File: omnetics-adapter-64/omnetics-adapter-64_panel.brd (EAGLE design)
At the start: 119 x 83 mm, 84 parts, among them J1 DF40-REC, J10 DF40-REC, J13 DF40-REC, J16 DF40-REC, J19 DF40-REC, J22 DF40-REC, J25 DF40-REC, J4 DF40-REC, J7 DF40-REC

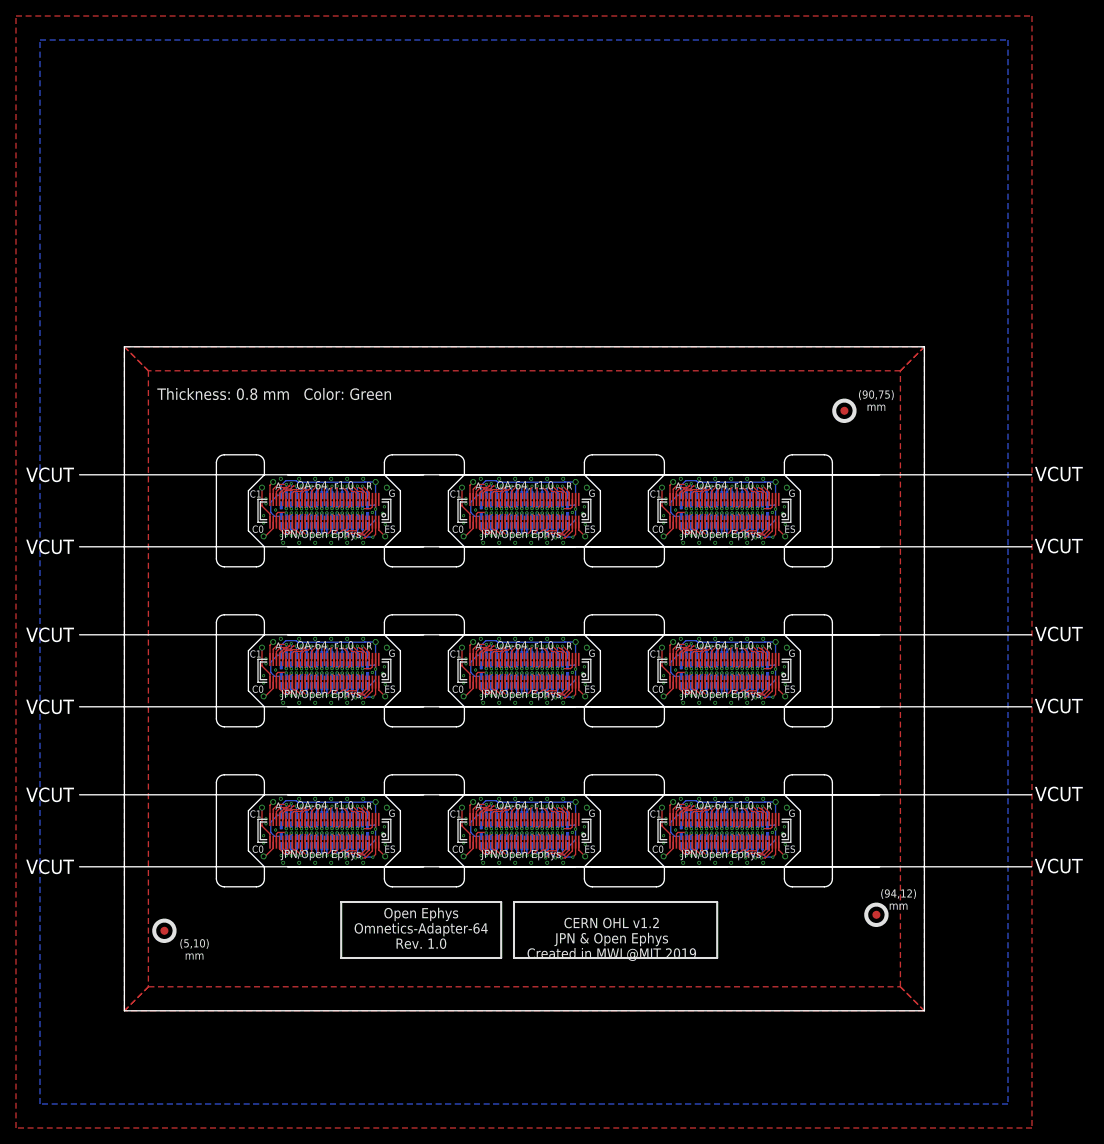
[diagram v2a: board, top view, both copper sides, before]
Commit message: headstage-64 rev. 1.4 along with all dependencies
- This is headstage-64 revision 1.4. Because it involves a change in the
bottom analog connector, a lot of other boards had to be changed to
match the new pinout. That is why there are so many files in this
commit. Changes in revision 1.4 and affects on other boards are as
follows:

1. The coaxial adapter board has been improved to allow a regulator to
sit on the daughter board. To do this, the filtered vcoax had to brought
back to the daughter board and then out again after regulation. Of
course this regulation can be bypassed simply by connecting these
contacts

2. Vcoax decoupling has been greatly improved to lower impedance of
power input. There is now 70 uF of decoupling capacitance on the
post-regulated vcoax.

3. The JTAG interface was changed to allow it to be enabled and disabled
by the programmer. This means that these pins are nominally used for
extra IO. The programmer now contains a jumper that allows it operate in
this new mode (closed) or legacy mode (open) for headstage-64 rev 1.3.

4. All of the serializers GPIO lines are now all routed to the FPGA.

5. The opto and estim circuits no longer share SPI lines so they can be
operated independently.

6. The analog routing to the intan chip has been changed such that the
electrode lines are shielded from vcoax, which was polluting the anlog
signals, by a ground pin. This means that eibs etc. need to respect this
new pinout. This is why eib-64, eib-64-large, nanoz-adapter,
omnetics-adapter-64, and test-board-64 have been changed.

7. The serializer on headstage-64 has been upgraded to DS90UB933-Q1
which has reduced back channel latencies, increased forward channel
bandwidth, and improved performance with
imperfect cabling.

8. There is a solder jumper on the bottom of headstage-64 to allow the
addition of an external resistor to AUXIN3 on the intan to allow it to
operate at lower bandwidths. This comes at the cost of not being able to
measure istim unless t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
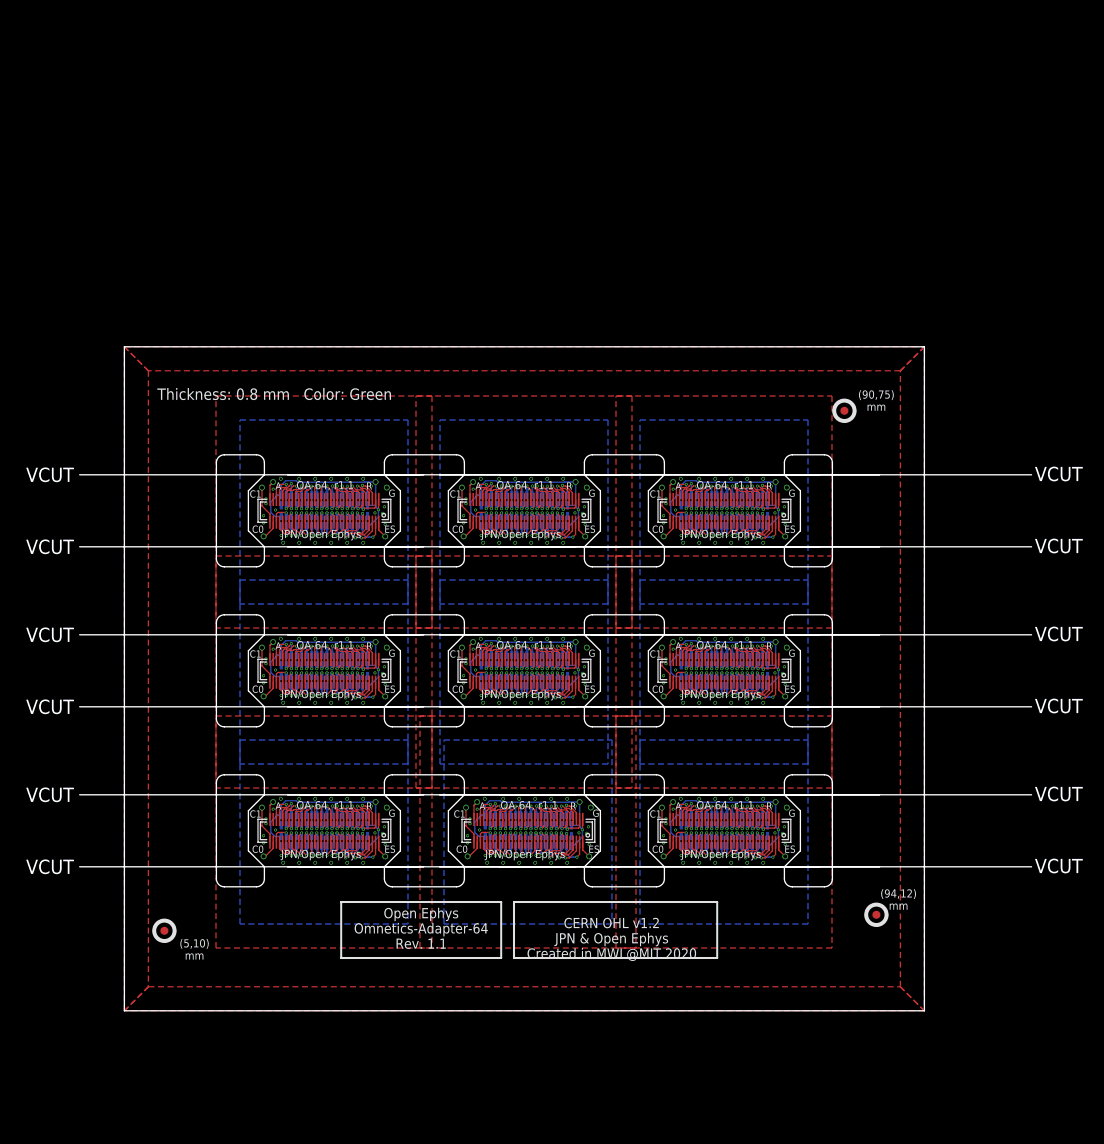
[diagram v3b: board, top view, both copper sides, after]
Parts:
- moved CAT12 50.0 mm to (67.4, 59.3)
- moved CAT16 50.0 mm to (17.4, 59.3)
- moved ESTIM19 50.0 mm to (81.4, 66.1)
- moved ESTIM25 50.0 mm to (31.4, 66.1)
- moved CAT13 50.0 mm to (67.2, 65.4)
- moved CAT17 50.0 mm to (17.2, 65.4)
- moved ESTIM20 50.0 mm to (82.8, 65.4)
- moved ESTIM26 50.0 mm to (32.8, 65.4)
- moved J19 50.0 mm to (75.0, 62.5)
- moved J25 50.0 mm to (25.0, 62.5)
- moved AN6 50.0 mm to (68.6, 66.1)
- moved AN8 50.0 mm to (18.6, 66.1)
- moved ESTIM18 50.0 mm to (82.6, 59.3)
- moved ESTIM24 50.0 mm to (32.6, 59.3)
- moved J20 50.0 mm to (69.6, 64.5)
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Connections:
- new net GND1: ESTIM2.P$1, J1.37, J2.18, J2.36, J3.18, J3.36
- new net GND2: ESTIM8.P$1, J7.37, J8.18, J8.36, J9.18, J9.36
- new net GND3: ESTIM11.P$1, J10.37, J11.18, J11.36, J12.18, J12.36
- new net GND4: ESTIM14.P$1, J13.37, J14.18, J14.36, J15.18, J15.36
- new net GND5: ESTIM17.P$1, J16.37, J17.18, J17.36, J18.18, J18.36
- new net GND6: ESTIM20.P$1, J19.37, J20.18, J20.36, J21.18, J21.36
- new net GND7: ESTIM23.P$1, J22.37, J23.18, J23.36, J24.18, J24.36
- new net GND8: ESTIM26.P$1, J25.37, J26.18, J26.36, J27.18, J27.36
- net GND: now also J4.37; no longer ESTIM11.P$1, ESTIM14.P$1, ESTIM17.P$1, ESTIM2.P$1, ESTIM20.P$1, ESTIM23.P$1, ESTIM26.P$1, ESTIM8.P$1, J1.70, J10.70, J11.18, J11.36, J12.18, J12.36, J13.70, J14.18, J14.36, J15.18, J15.36, J16.70, J17.18, J17.36, J18.18, J18.36, J19.70, J2.18, J2.36, J20.18, J20.36, J21.18, J21.36, J22.70, J23.18, J23.36, J24.18, J24.36, J25.70, J26.18, J26.36, J27.18, J27.36, J3.18, J3.36, J4.70, J7.70, J8.18, J8.36, J9.18, J9.36
- net N$1: now also J1.69; no longer J1.68
- net N$100: now also J4.38; no longer J4.37
- net N$12: now also J1.60; no longer J1.57
- net N$129: now also J7.69; no longer J7.68
- net N$130: now also J7.67; no longer J7.66
- net N$131: now also J7.65; no longer J7.64
- net N$132: now also J7.64; no longer J7.63
- net N$133: now also J7.63; no longer J7.62
- net N$135: now also J7.62; no longer J7.60
- net N$138: now also J7.60; no longer J7.57
- net N$14: now also J1.57; no longer J1.55
- net N$140: now also J7.57; no longer J7.55
- net N$142: now also J7.55; no longer J7.53
- net N$143: now also J7.53; no longer J7.52
- net N$144: now also J7.52; no longer J7.51
- net N$145: now also J7.51; no longer J7.50
- net N$146: now also J7.50; no longer J7.49
- net N$147: now also J7.49; no longer J7.48
- net N$148: now also J7.48; no longer J7.47
- net N$149: now also J7.47; no longer J7.46
- net N$150: now also J7.46; no longer J7.45
- net N$151: now also J7.45; no longer J7.44
- net N$152: now also J7.44; no longer J7.43
- net N$153: now also J7.43; no longer J7.42
- net N$154: now also J7.42; no longer J7.41
- net N$155: now also J7.41; no longer J7.40
- net N$156: now also J7.39; no longer J7.38
- net N$16: now also J1.55; no longer J1.53
- net N$161: now also J7.66; no longer J7.65
- net N$162: now also J7.68; no longer J7.67
- net N$163: now also J7.40; no longer J7.39
- net N$164: now also J7.38; no longer J7.37
- net N$17: now also J1.53; no longer J1.52
- net N$18: now also J1.52; no longer J1.51
- net N$19: now also J1.51; no longer J1.50
- net N$193: now also J10.69; no longer J10.68
- net N$194: now also J10.67; no longer J10.66
- net N$195: now also J10.65; no longer J10.64
- net N$196: now also J10.64; no longer J10.63
- net N$197: now also J10.63; no longer J10.62
- net N$199: now also J10.62; no longer J10.60
- net N$2: now also J1.66; no longer J1.65
- net N$20: now also J1.50; no longer J1.49
- net N$21: now also J1.49; no longer J1.48
- net N$22: now also J1.48; no longer J1.47
- net N$229: now also J10.60; no longer J10.57
- net N$23: now also J1.47; no longer J1.46
- net N$231: now also J10.57; no longer J10.55
- net N$233: now also J10.55; no longer J10.53
- net N$234: now also J10.53; no longer J10.52
- net N$235: now also J10.52; no longer J10.51
- net N$236: now also J10.51; no longer J10.50
- net N$237: now also J10.50; no longer J10.49
- net N$238: now also J10.49; no longer J10.48
- net N$239: now also J10.48; no longer J10.47
- net N$24: now also J1.46; no longer J1.45
- net N$240: now also J10.47; no longer J10.46
- net N$241: now also J10.46; no longer J10.45
- net N$242: now also J10.45; no longer J10.44
- net N$243: now also J10.44; no longer J10.43
- net N$244: now also J10.43; no longer J10.42
- net N$245: now also J10.42; no longer J10.41
- net N$246: now also J10.41; no longer J10.40
- net N$247: now also J10.39; no longer J10.38
- net N$25: now also J1.45; no longer J1.44
- net N$252: now also J10.66; no longer J10.65
- net N$253: now also J10.68; no longer J10.67
- net N$254: now also J10.40; no longer J10.39
- net N$255: now also J10.38; no longer J10.37
- net N$26: now also J1.44; no longer J1.43
- net N$27: now also J1.43; no longer J1.42
- net N$28: now also J1.42; no longer J1.41
- net N$284: now also J13.69; no longer J13.68
- net N$285: now also J13.67; no longer J13.66
- net N$286: now also J13.65; no longer J13.64
- net N$287: now also J13.64; no longer J13.63
- net N$288: now also J13.63; no longer J13.62
- net N$29: now also J1.41; no longer J1.40
- net N$290: now also J13.62; no longer J13.60
- net N$293: now also J13.60; no longer J13.57
- net N$295: now also J13.57; no longer J13.55
- net N$297: now also J13.55; no longer J13.53
- net N$298: now also J13.53; no longer J13.52
- net N$299: now also J13.52; no longer J13.51
- net N$3: now also J1.67; no longer J1.66
- net N$30: now also J1.40; no longer J1.39
- net N$300: now also J13.51; no longer J13.50
- net N$301: now also J13.50; no longer J13.49
- net N$302: now also J13.49; no longer J13.48
- net N$303: now also J13.48; no longer J13.47
- net N$304: now also J13.47; no longer J13.46
- net N$305: now also J13.46; no longer J13.45
- net N$306: now also J13.45; no longer J13.44
- net N$307: now also J13.44; no longer J13.43
- net N$308: now also J13.43; no longer J13.42
- net N$309: now also J13.42; no longer J13.41
- net N$31: now also J1.39; no longer J1.38
- net N$310: now also J13.41; no longer J13.40
- net N$311: now also J13.39; no longer J13.38
- net N$316: now also J13.66; no longer J13.65
- net N$317: now also J13.68; no longer J13.67
- net N$318: now also J13.40; no longer J13.39
- net N$319: now also J13.38; no longer J13.37
- net N$32: now also J1.38; no longer J1.37
- net N$348: now also J16.69; no longer J16.68
- net N$349: now also J16.67; no longer J16.66
- net N$350: now also J16.65; no longer J16.64
- net N$351: now also J16.64; no longer J16.63
- net N$352: now also J16.63; no longer J16.62
- net N$354: now also J16.62; no longer J16.60
- net N$357: now also J16.60; no longer J16.57
- net N$359: now also J16.57; no longer J16.55
- net N$361: now also J16.55; no longer J16.53
- net N$362: now also J16.53; no longer J16.52
- net N$363: now also J16.52; no longer J16.51
- net N$364: now also J16.51; no longer J16.50
- net N$365: now also J16.50; no longer J16.49
- net N$366: now also J16.49; no longer J16.48
- net N$367: now also J16.48; no longer J16.47
- net N$368: now also J16.47; no longer J16.46
- net N$369: now also J16.46; no longer J16.45
- net N$370: now also J16.45; no longer J16.44
- net N$371: now also J16.44; no longer J16.43
- net N$372: now also J16.43; no longer J16.42
- net N$373: now also J16.42; no longer J16.41
- net N$374: now also J16.41; no longer J16.40
- net N$375: now also J16.39; no longer J16.38
- net N$380: now also J16.66; no longer J16.65
- net N$381: now also J16.68; no longer J16.67
- net N$382: now also J16.40; no longer J16.39
- net N$383: now also J16.38; no longer J16.37
- net N$4: now also J1.68; no longer J1.67
- net N$412: now also J19.69; no longer J19.68
- net N$413: now also J19.67; no longer J19.66
- net N$414: now also J19.65; no longer J19.64
- net N$415: now also J19.64; no longer J19.63
- net N$416: now also J19.63; no longer J19.62
- net N$418: now also J19.62; no longer J19.60
- net N$421: now also J19.60; no longer J19.57
- net N$423: now also J19.57; no longer J19.55
- net N$425: now also J19.55; no longer J19.53
- net N$426: now also J19.53; no longer J19.52
- net N$427: now also J19.52; no longer J19.51
- net N$428: now also J19.51; no longer J19.50
- net N$429: now also J19.50; no longer J19.49
- net N$430: now also J19.49; no longer J19.48
- net N$431: now also J19.48; no longer J19.47
- net N$432: now also J19.47; no longer J19.46
- net N$433: now also J19.46; no longer J19.45
- net N$434: now also J19.45; no longer J19.44
- net N$435: now also J19.44; no longer J19.43
- net N$436: now also J19.43; no longer J19.42
- net N$437: now also J19.42; no longer J19.41
- net N$438: now also J19.41; no longer J19.40
- net N$439: now also J19.39; no longer J19.38
- net N$444: now also J19.66; no longer J19.65
- net N$445: now also J19.68; no longer J19.67
- net N$446: now also J19.40; no longer J19.39
- net N$447: now also J19.38; no longer J19.37
- net N$476: now also J22.69; no longer J22.68
- net N$477: now also J22.67; no longer J22.66
- net N$478: now also J22.65; no longer J22.64
- net N$479: now also J22.64; no longer J22.63
- net N$480: now also J22.63; no longer J22.62
- net N$482: now also J22.62; no longer J22.60
- net N$485: now also J22.60; no longer J22.57
- net N$487: now also J22.57; no longer J22.55
- net N$489: now also J22.55; no longer J22.53
- net N$490: now also J22.53; no longer J22.52
- net N$491: now also J22.52; no longer J22.51
- net N$492: now also J22.51; no longer J22.50
- net N$493: now also J22.50; no longer J22.49
- net N$494: now also J22.49; no longer J22.48
- net N$495: now also J22.48; no longer J22.47
- net N$496: now also J22.47; no longer J22.46
- net N$497: now also J22.46; no longer J22.45
- net N$498: now also J22.45; no longer J22.44
- net N$499: now also J22.44; no longer J22.43
- net N$5: now also J1.65; no longer J1.64
- net N$500: now also J22.43; no longer J22.42
- net N$501: now also J22.42; no longer J22.41
- net N$502: now also J22.41; no longer J22.40
- net N$503: now also J22.39; no longer J22.38
- net N$508: now also J22.66; no longer J22.65
- net N$509: now also J22.68; no longer J22.67
- net N$510: now also J22.40; no longer J22.39
- net N$511: now also J22.38; no longer J22.37
- net N$540: now also J25.69; no longer J25.68
- net N$541: now also J25.67; no longer J25.66
- net N$542: now also J25.65; no longer J25.64
- net N$543: now also J25.64; no longer J25.63
- net N$544: now also J25.63; no longer J25.62
- net N$546: now also J25.62; no longer J25.60
- net N$549: now also J25.60; no longer J25.57
- net N$551: now also J25.57; no longer J25.55
- net N$553: now also J25.55; no longer J25.53
- net N$554: now also J25.53; no longer J25.52
- net N$555: now also J25.52; no longer J25.51
- net N$556: now also J25.51; no longer J25.50
- net N$557: now also J25.50; no longer J25.49
- net N$558: now also J25.49; no longer J25.48
- net N$559: now also J25.48; no longer J25.47
- net N$560: now also J25.47; no longer J25.46
- net N$561: now also J25.46; no longer J25.45
- net N$562: now also J25.45; no longer J25.44
- net N$563: now also J25.44; no longer J25.43
- net N$564: now also J25.43; no longer J25.42
- net N$565: now also J25.42; no longer J25.41
- net N$566: now also J25.41; no longer J25.40
- net N$567: now also J25.39; no longer J25.38
- net N$572: now also J25.66; no longer J25.65
- net N$573: now also J25.68; no longer J25.67
- net N$574: now also J25.40; no longer J25.39
- net N$575: now also J25.38; no longer J25.37
- net N$6: now also J1.64; no longer J1.63
- net N$65: now also J4.69; no longer J4.68
- net N$66: now also J4.67; no longer J4.66
- net N$67: now also J4.65; no longer J4.64
- net N$68: now also J4.64; no longer J4.63
- net N$69: now also J4.63; no longer J4.62
- net N$7: now also J1.63; no longer J1.62
- net N$71: now also J4.62; no longer J4.60
- net N$74: now also J4.60; no longer J4.57
- net N$76: now also J4.57; no longer J4.55
- net N$78: now also J4.55; no longer J4.53
- net N$79: now also J4.53; no longer J4.52
- net N$80: now also J4.52; no longer J4.51
- net N$81: now also J4.51; no longer J4.50
- net N$82: now also J4.50; no longer J4.49
- net N$83: now also J4.49; no longer J4.48
- net N$84: now also J4.48; no longer J4.47
- net N$85: now also J4.47; no longer J4.46
- net N$86: now also J4.46; no longer J4.45
- net N$87: now also J4.45; no longer J4.44
- net N$88: now also J4.44; no longer J4.43
- net N$89: now also J4.43; no longer J4.42
- net N$9: now also J1.62; no longer J1.60
- net N$90: now also J4.42; no longer J4.41
- net N$91: now also J4.41; no longer J4.40
- net N$92: now also J4.39; no longer J4.38
- net N$97: now also J4.66; no longer J4.65
- net N$98: now also J4.68; no longer J4.67
- net N$99: now also J4.40; no longer J4.39
- net REF: now also J1.70; no longer J1.69
- net REF1: now also J4.70; no longer J4.69
- net REF2: now also J7.70; no longer J7.69
- net REF3: now also J10.70; no longer J10.69
- net REF4: now also J13.70; no longer J13.69
- net REF5: now also J16.70; no longer J16.69
- net REF6: now also J19.70; no longer J19.69
- net REF7: now also J22.70; no longer J22.69
- net REF8: now also J25.70; no longer J25.69
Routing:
- net N$437: track 3.48 -> 1.73 mm
- net N$90: track 3.48 -> 1.73 mm
- net N$373: track 3.48 -> 1.73 mm
- net N$154: track 3.48 -> 1.73 mm
- net N$28: track 3.48 -> 1.73 mm
- net N$565: track 3.48 -> 1.73 mm
- net N$501: track 3.48 -> 1.73 mm
- net N$245: track 3.48 -> 1.73 mm
- net N$309: track 3.48 -> 1.73 mm
- net N$241: track 2.81 -> 1.59 mm
- net N$561: track 2.81 -> 1.59 mm
- net N$305: track 2.81 -> 1.59 mm
- net N$497: track 2.81 -> 1.59 mm
- net N$369: track 2.81 -> 1.59 mm
- net N$150: track 2.81 -> 1.59 mm
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- added copper zone on layer 1, net GND1
- added copper zone on layer 16, net GND1
- added copper zone on layer 1, net GND2
- added copper zone on layer 16, net GND2
- added copper zone on layer 1, net GND3
- added copper zone on layer 16, net GND3
- added copper zone on layer 1, net GND4
- added copper zone on layer 16, net GND4
- added copper zone on layer 1, net GND5
- added copper zone on layer 16, net GND5
- added copper zone on layer 1, net GND6
- added copper zone on layer 16, net GND6
- added copper zone on layer 1, net GND7
- added copper zone on layer 16, net GND7
- added copper zone on layer 1, net GND8
- added copper zone on layer 16, net GND8
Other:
- board text added: "CERN OHL v1.2 JPN & Open Ephys Created in MWL@MIT 2020"
- board text added: "OA-64, r1.1"
- board text added: "Open Ephys Omnetics-Adapter-64 Rev. 1.1"
- board text removed: "CERN OHL v1.2 JPN & Open Ephys Created in MWL@MIT 2019"
- board text removed: "OA-64, r1.0"
- board text removed: "Open Ephys Omnetics-Adapter-64 Rev. 1.0"

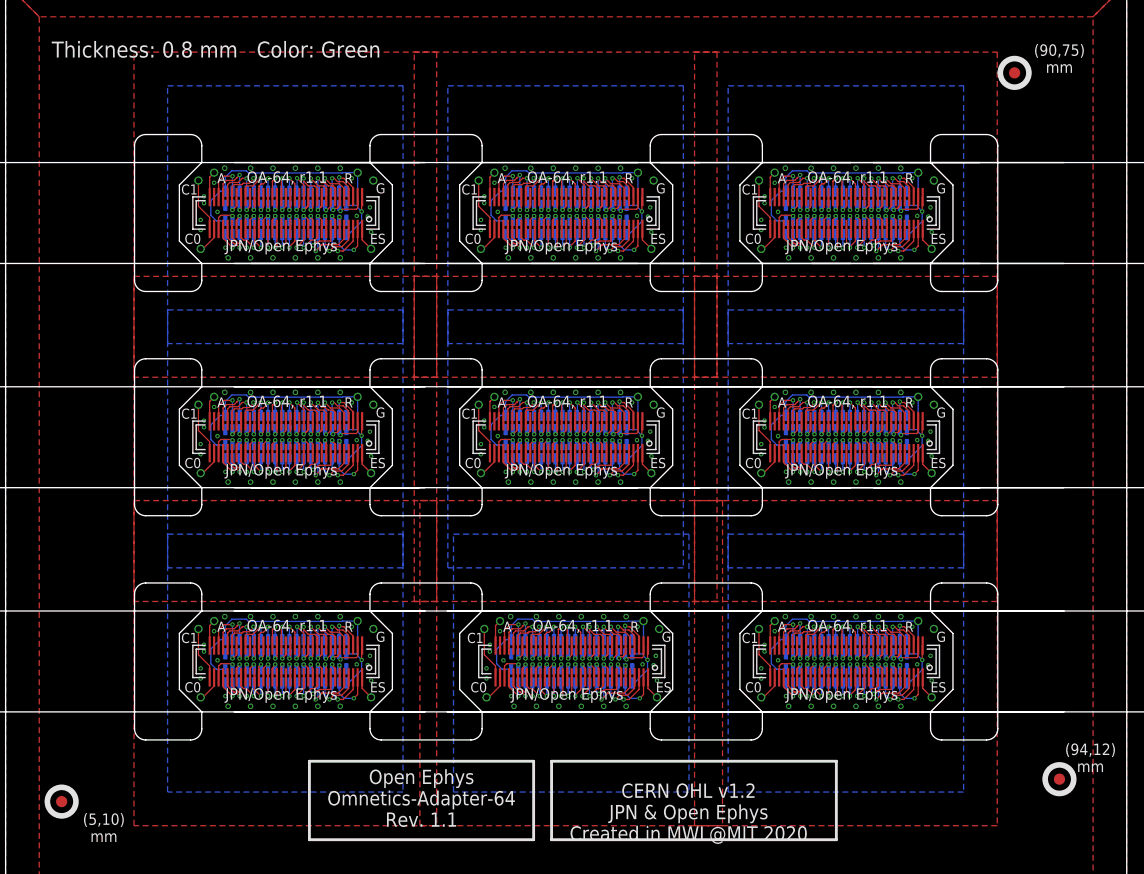
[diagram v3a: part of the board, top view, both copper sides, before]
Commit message: Added fiducial marks to the bottom of omnetics-adapter-64 board
- This board has bottom side components so these are needed
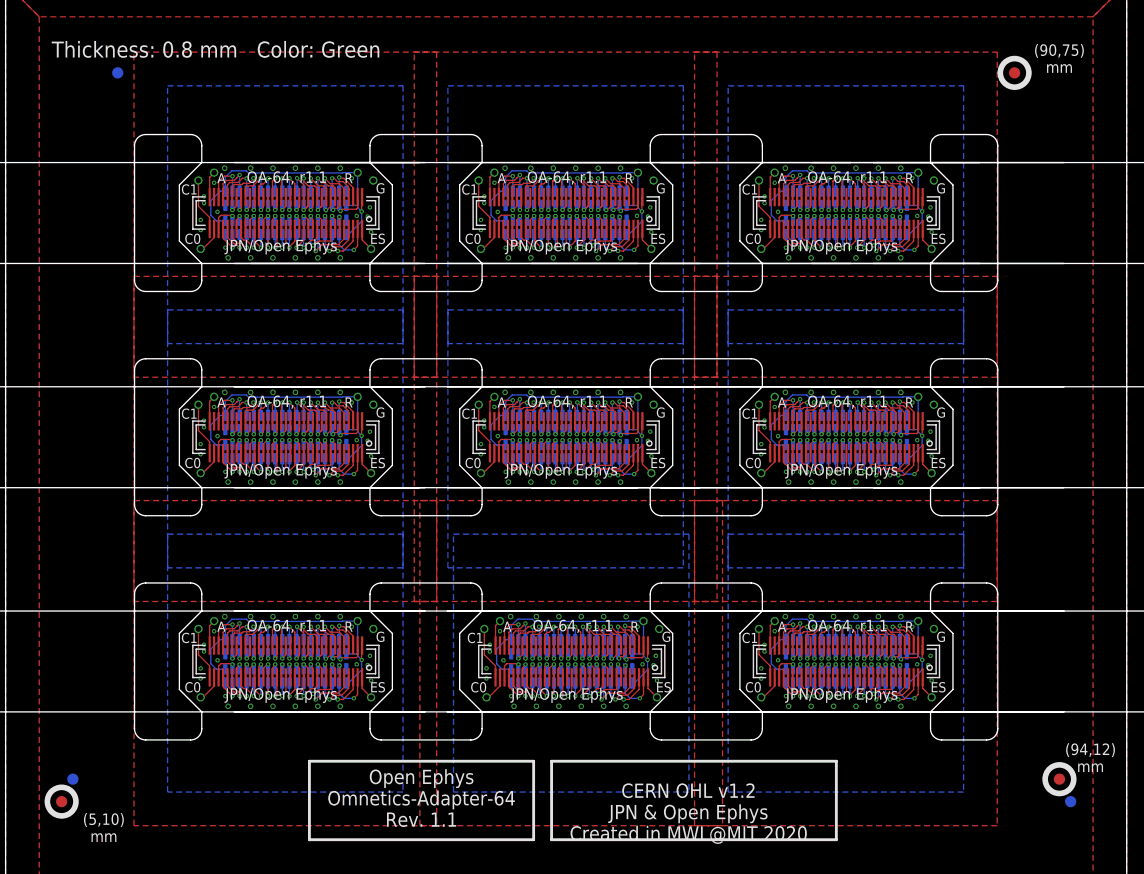
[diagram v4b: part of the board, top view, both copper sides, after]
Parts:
- added E$4, E$5, E$6: (no value), fiducial:FIDUCIAL
